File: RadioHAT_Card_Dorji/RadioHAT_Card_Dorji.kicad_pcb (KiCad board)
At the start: 2 copper layers, 30 x 51 mm, 10 parts, among them J2 Conn_Coaxial, J3 Conn_Coaxial, J4 Conn_Coaxial, J5 Conn_Coaxial, J6 Conn_Coaxial

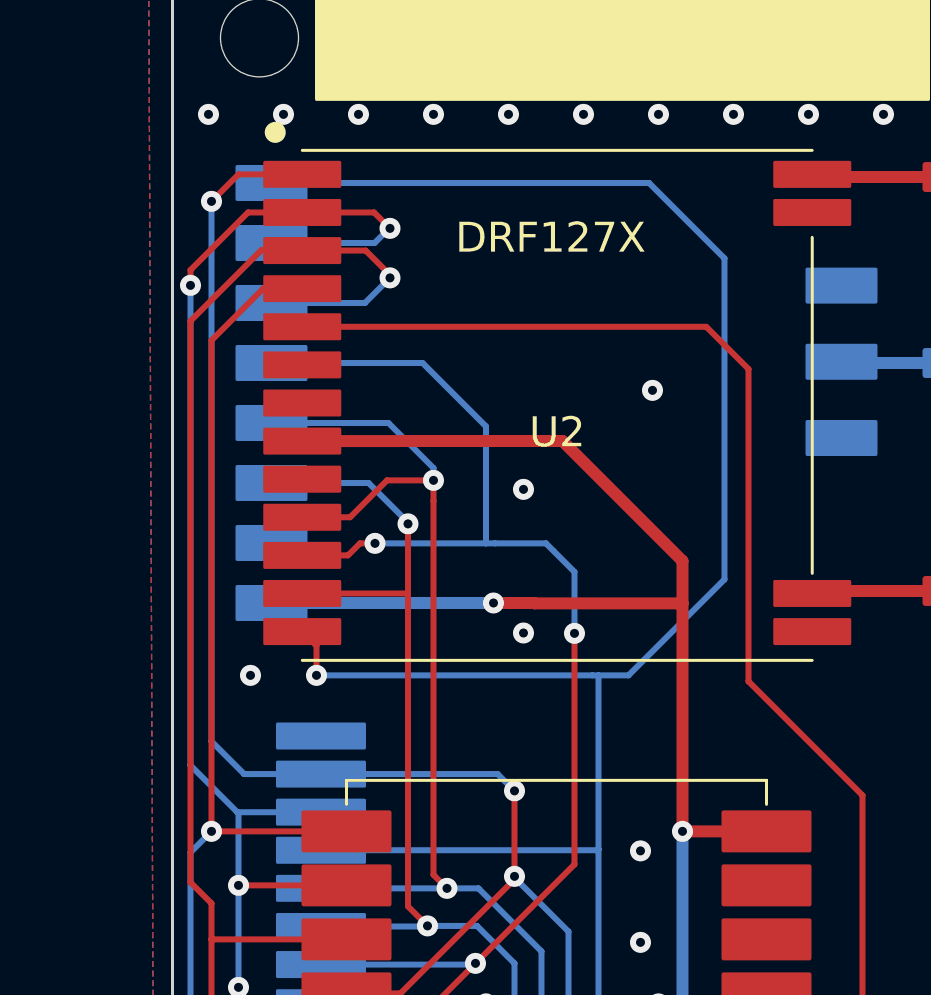
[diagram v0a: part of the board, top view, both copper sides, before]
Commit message: [PCB] Update footprints
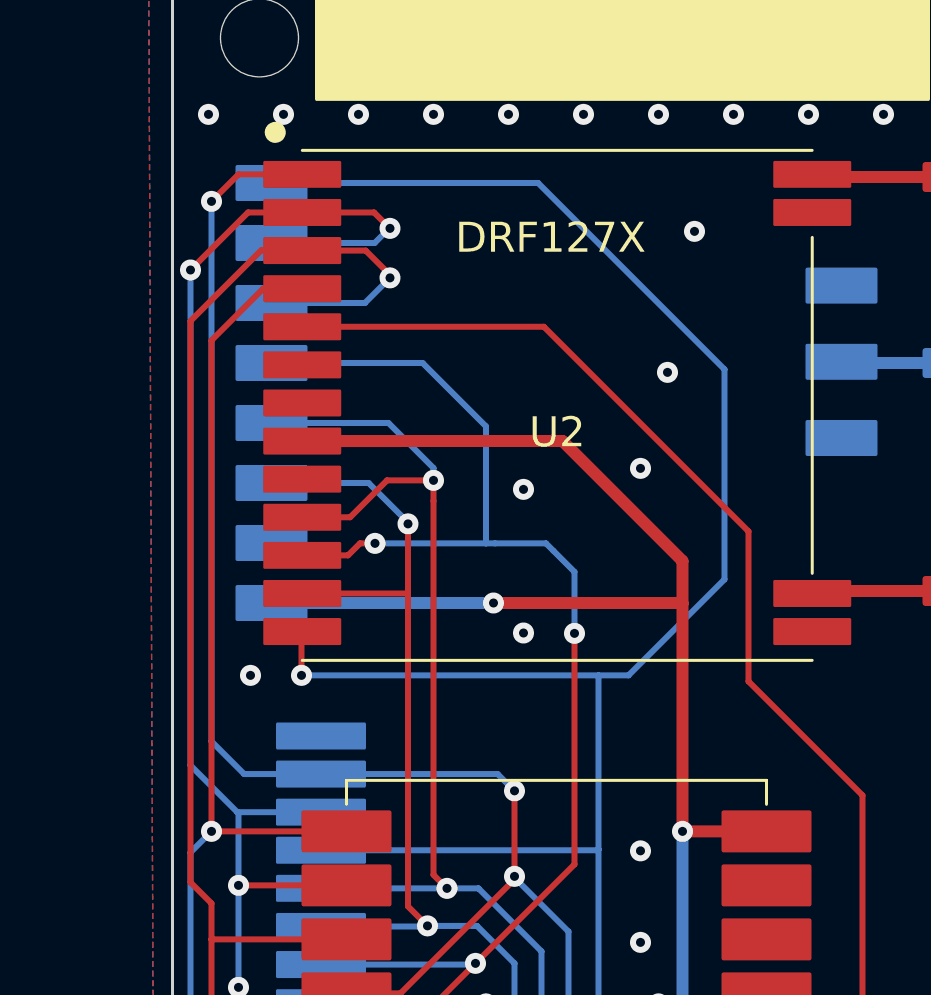
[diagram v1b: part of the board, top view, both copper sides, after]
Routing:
- net GPIO1: track 72.1 -> 68.9 mm
- net NSS: track 98.2 -> 96.2 mm
- net GND: vias 31 -> 33
